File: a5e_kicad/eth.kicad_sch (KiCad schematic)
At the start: 58 parts, among them J9 RJ45_RB1-125B8G1A, U10 RTL8211FDI-CG, Y3 25MHz

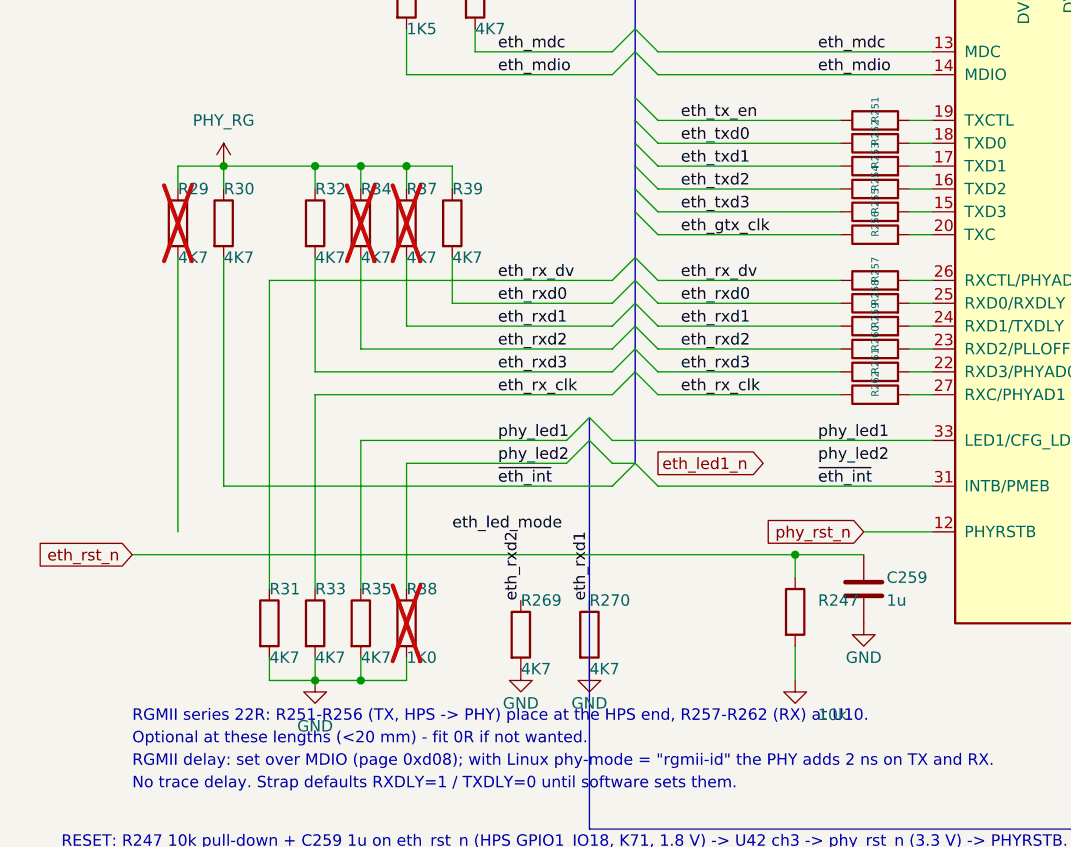
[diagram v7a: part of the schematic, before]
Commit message: Remove PHY swap leftovers R38/R29 (schematic and PCB), NC flags on bank 6C C19/H16
R38 1K0 had pin 1 alone on phy_led2, R29 4K7 pin 2 unconnected. Also removes the dead PHY LED2 labels,
bus entries and the orphan R29 pad-2 track. Netlist: only R29/R38 pins gone; DRC parity 0.
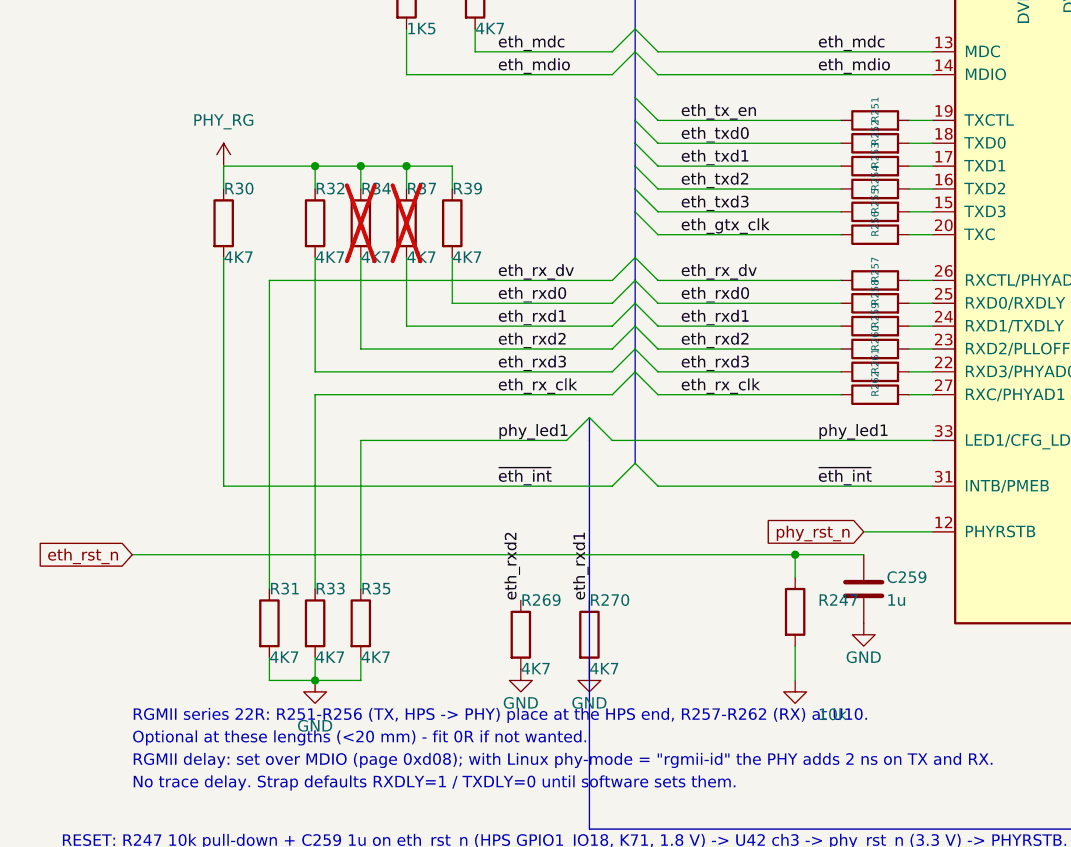
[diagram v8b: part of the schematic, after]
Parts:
- removed R29: 4K7, Resistor_SMD:R_0402_1005Metric, symbol Device:R
- removed R38: 1K0, Resistor_SMD:R_0402_1005Metric, symbol Device:R
